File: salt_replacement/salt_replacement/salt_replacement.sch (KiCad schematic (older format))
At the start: 18 parts, among them J1 SALT chip package pins, U1 IC REG BUCK SEPIC 5V 4.5A 8SO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, U2 MAX3232

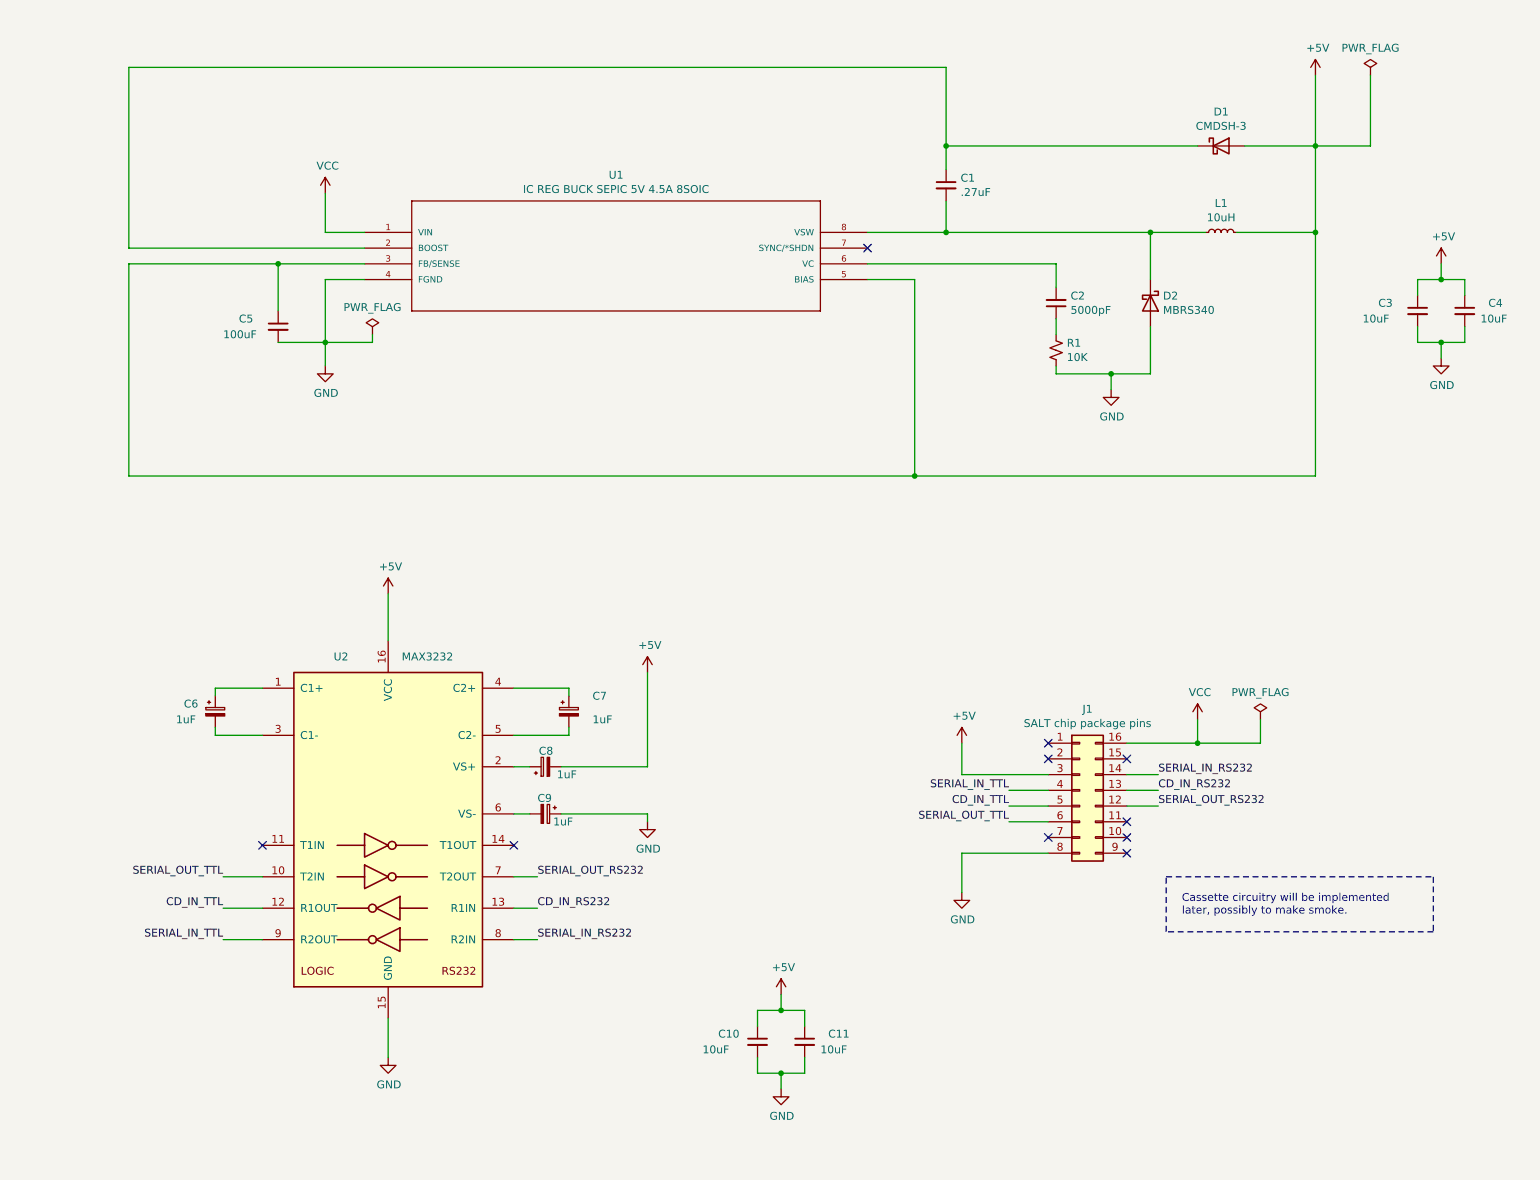
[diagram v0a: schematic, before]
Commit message: -added more components -started making the PCB
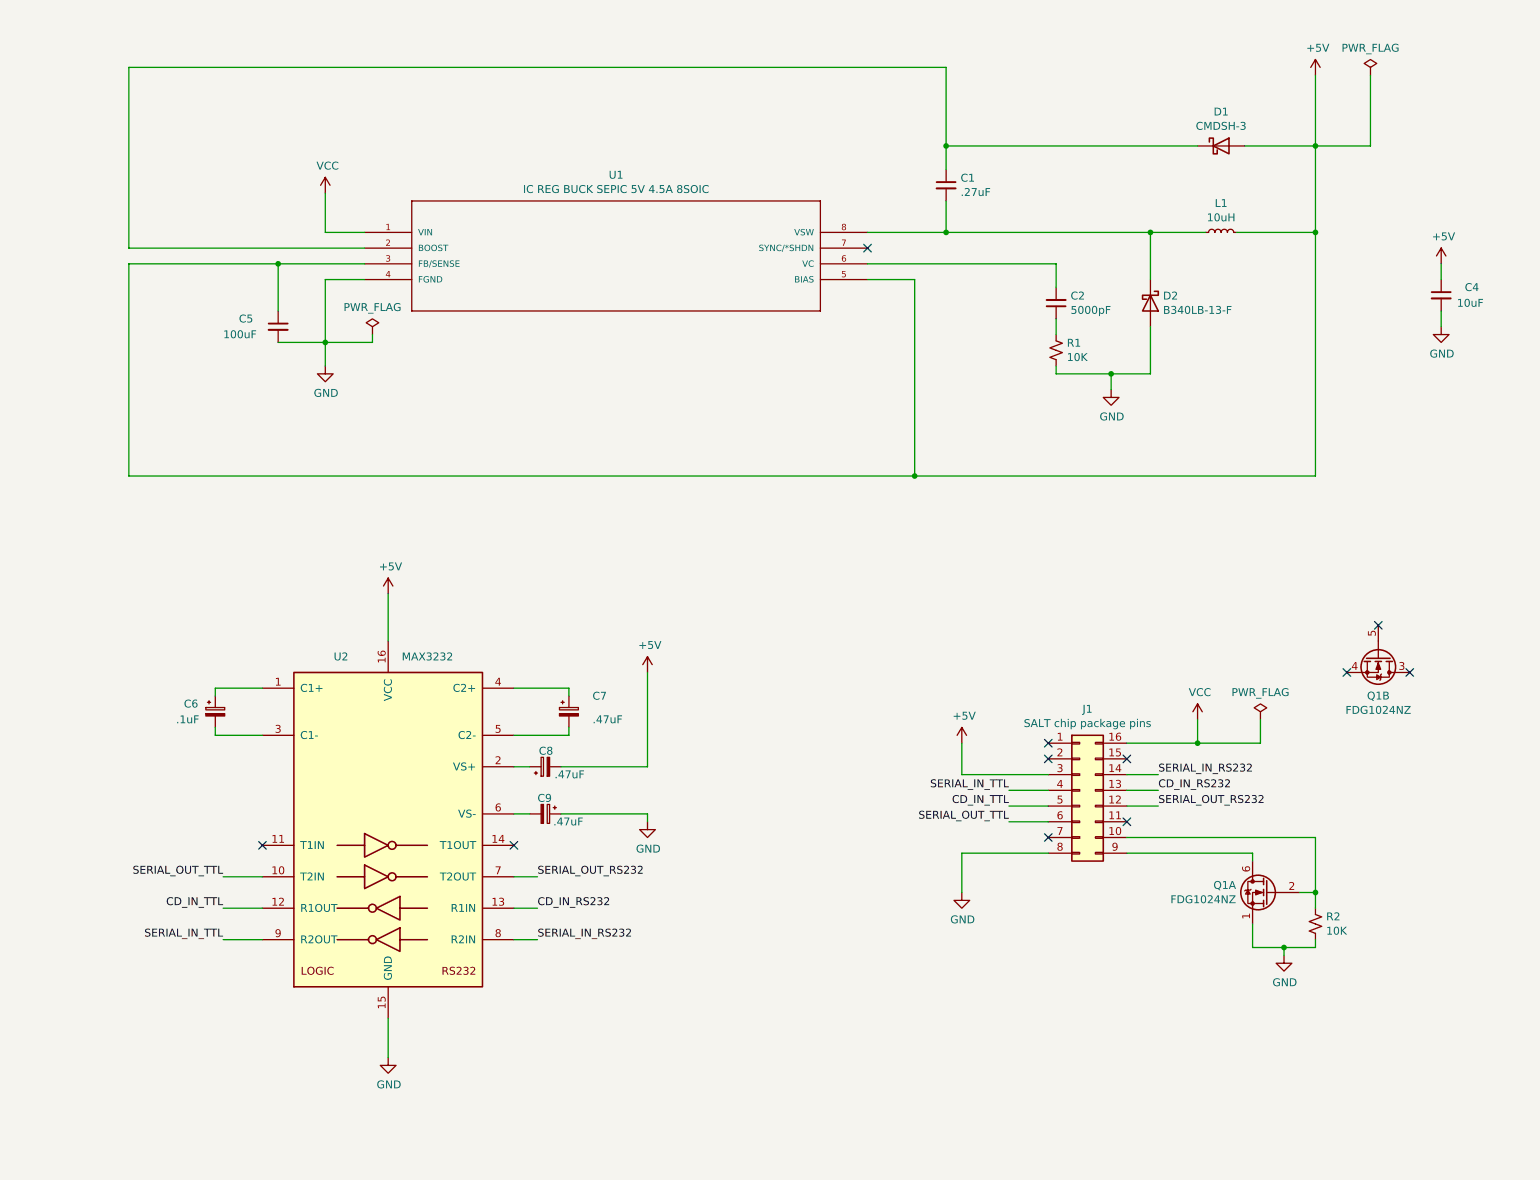
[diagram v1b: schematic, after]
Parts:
- removed C10, C11, C3: 10uF, symbol Device:C_Small
- added Q1: FDG1024NZ, Package_TO_SOT_SMD:SOT-363_SC-70-6, symbol Transistor_FET:FDG1024NZ
- added R2: 10K, Resistor_SMD:R_0805_2012Metric_Pad1.20x1.40mm_HandSolder, symbol Device:R_Small_US
- C1: footprint (none) -> Capacitor_SMD:C_1206_3216Metric_Pad1.33x1.80mm_HandSolder; Manufacturer part# (none) -> 12065C274KAT2A; Vendor (none) -> Digikey; Vendor part# (none) -> 478-1561-1-ND
- C2: footprint (none) -> Capacitor_SMD:C_0805_2012Metric_Pad1.18x1.45mm_HandSolder; Manufacturer part# (none) -> 08055C502KAT2A; Vendor (none) -> Digikey; Vendor part# (none) -> 478-10560-1-ND
- C4: footprint (none) -> Capacitor_Tantalum_SMD:CP_EIA-3216-18_Kemet-A_Pad1.58x1.35mm_HandSolder; Manufacturer part# (none) -> T491A106K010AT; Vendor (none) -> digikey; Vendor part# (none) -> 399-3684-1-ND
- C5: footprint (none) -> Capacitor_Tantalum_SMD:CP_EIA-7343-31_Kemet-D_Pad2.25x2.55mm_HandSolder; Vendor (none) -> digikey; Vendor part# (none) -> 478-9137-1-ND; manufacturer part# (none) -> TPSD107K010S0080
- C6: value 1uF -> .1uF; footprint (none) -> Capacitor_SMD:C_0603_1608Metric_Pad1.08x0.95mm_HandSolder; Manufacturer part# (none) -> CC0603KRX7R9BB104; Vendor (none) -> digikey; Vendor part# (none) -> 311-1344-1-ND
- C7, C8, C9: value 1uF -> .47uF; footprint (none) -> Capacitor_SMD:C_0603_1608Metric_Pad1.08x0.95mm_HandSolder; Manufacturer part# (none) -> C0603C474K4RACTU; Vendor (none) -> digikey; Vendor part# (none) -> 399-4922-1-ND
- D1: footprint (none) -> Diode_SMD:D_SOD-323_HandSoldering; Manufacturer part# (none) -> CMDSH-3 TR PBFREE; Vendor (none) -> Digikey; Vendor part# (none) -> 1514-CMDSH-3TRPBFREECT-ND
- D2: value MBRS340 -> B340LB-13-F; footprint (none) -> Diode_SMD:D_SMC; Manufacturer part# (none) -> B340LB-13-F; Vendor (none) -> digikey; Vendor part# (none) -> B340LB-FDICT-ND
- J1: footprint (none) -> Package_DIP:DIP-16_W7.62mm_Socket
- L1: footprint (none) -> salt_replacement:L_Sumida_CDMC6D28_7.25x6.5mm; Manufacturer part# (none) -> SRP6540-100M; Vendor (none) -> Digikey; Vendor part# (none) -> SRP6540-100MCT-ND
- R1: footprint (none) -> Resistor_SMD:R_0805_2012Metric_Pad1.20x1.40mm_HandSolder; Manufacturer part# (none) -> RK73B2ATTD103J; Vendor (none) -> digikey; Vendor part# (none) -> 2019-RK73B2ATTD103JCT-ND
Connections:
- net GND: now also Q1.1 (S), R2.2
- net at J1.10 (Pin_10): now also Q1.2 (G), R2.1
- net at J1.9 (Pin_9): now also Q1.6 (D)
- no-connect marks 10 -> 11
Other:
- note removed: "Cassette circuitry will be implemented\nlater, possibly to make smoke."
- moved on the sheet: C4

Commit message: -complete redesign -replaced all components with jclpcb stock -added non-inverting zero crossing circuit.
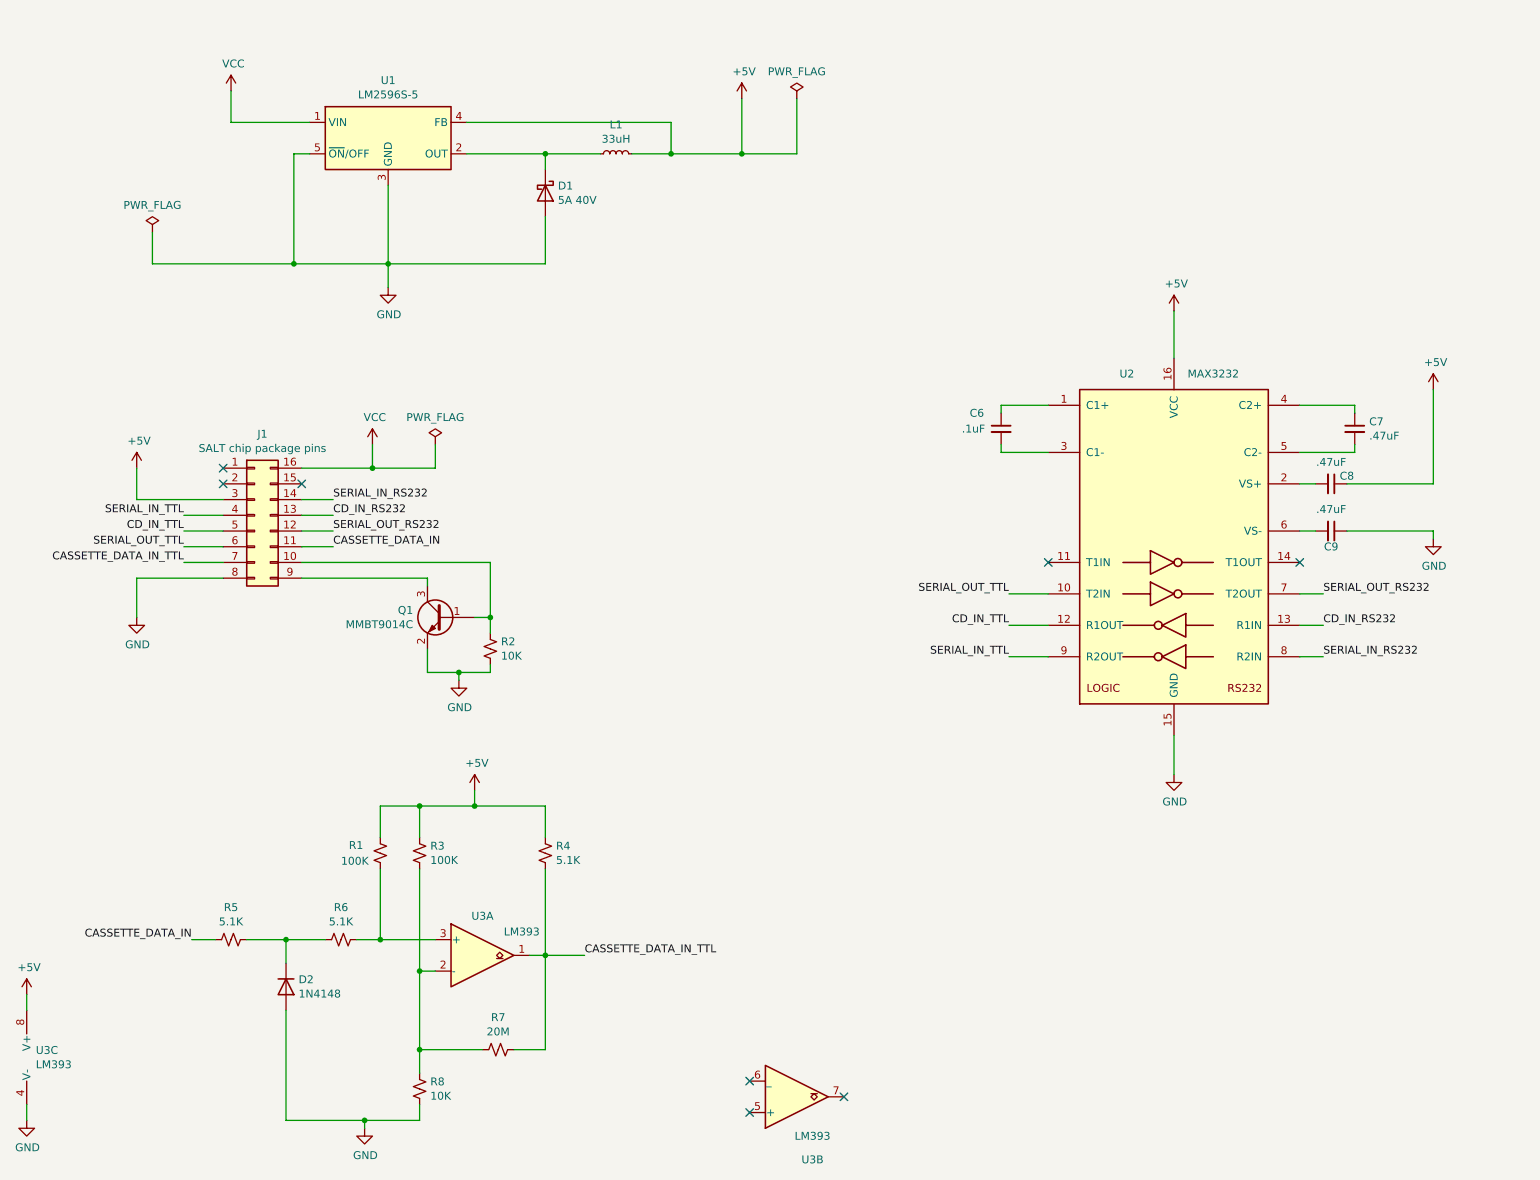
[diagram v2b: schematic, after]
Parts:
- removed C1: .27uF, Capacitor_SMD:C_1206_3216Metric_Pad1.33x1.80mm_HandSolder, symbol Device:C_Small
- removed C2: 5000pF, Capacitor_SMD:C_0805_2012Metric_Pad1.18x1.45mm_HandSolder, symbol Device:C_Small
- removed C4: 10uF, Capacitor_Tantalum_SMD:CP_EIA-3216-18_Kemet-A_Pad1.58x1.35mm_HandSolder, symbol Device:C_Small
- removed C5: 100uF, Capacitor_Tantalum_SMD:CP_EIA-7343-31_Kemet-D_Pad2.25x2.55mm_HandSolder, symbol Device:C_Small
- removed C6: .1uF, Capacitor_SMD:C_0603_1608Metric_Pad1.08x0.95mm_HandSolder, symbol Device:CP_Small
- removed C7, C8, C9: .47uF, Capacitor_SMD:C_0603_1608Metric_Pad1.08x0.95mm_HandSolder, symbol Device:CP_Small
- removed D2: B340LB-13-F, Diode_SMD:D_SMC, symbol Device:D_Schottky
- removed Q1: FDG1024NZ, Package_TO_SOT_SMD:SOT-363_SC-70-6, symbol Transistor_FET:FDG1024NZ
- removed U1: IC REG BUCK SEPIC 5V 4.5A 8SOIC, Package_SO:SO-8_3.9x4.9mm_P1.27mm, symbol coco_rip:LT1374CS8-5PBF
- added C6: .1uF, Capacitor_SMD:C_0402_1005Metric, symbol Device:C_Small
- added C7, C8, C9: .47uF, Capacitor_SMD:C_0603_1608Metric, symbol Device:C_Small
- added D2: 1N4148, Diode_SMD:D_SOD-523, symbol Diode:1N4148
- added Q1: MMBT9014C, Package_TO_SOT_SMD:SOT-23, symbol Transistor_BJT:BC818
- added R3: 100K, Resistor_SMD:R_0402_1005Metric, symbol Device:R_Small_US
- added R4, R5, R6: 5.1K, Resistor_SMD:R_0402_1005Metric, symbol Device:R_Small_US
- added R7: 20M, Resistor_SMD:R_0402_1005Metric, symbol Device:R_Small_US
- added R8: 10K, Resistor_SMD:R_0402_1005Metric, symbol Device:R_Small_US
- added U1: LM2596S-5, Package_TO_SOT_SMD:TO-263-5_TabPin3, symbol Regulator_Switching:LM2596S-5
- added U3: LM393, Package_SO:TSSOP-8_4.4x3mm_P0.65mm, symbol Comparator:LM393
- D1: value CMDSH-3 -> 5A 40V; footprint Diode_SMD:D_SOD-323_HandSoldering -> Diode_SMD:D_SMB; Manufacturer part# CMDSH-3 TR PBFREE -> SS54B; Vendor Digikey -> LCSC; Vendor part# 1514-CMDSH-3TRPBFREECT-ND -> C32513
- J1: Manufacturer part# (none) -> DNI; Vendor (none) -> DNI; Vendor part# (none) -> DNI
- L1: value 10uH -> 33uH; footprint salt_replacement:L_Sumida_CDMC6D28_7.25x6.5mm -> Inductor_SMD:L_Sumida_CDMC6D28_7.25x6.5mm; Manufacturer part# SRP6540-100M -> MHCI06030-330M-R8; Vendor Digikey -> LSCSC; Vendor part# SRP6540-100MCT-ND -> C329385
- R1: value 10K -> 100K; footprint Resistor_SMD:R_0805_2012Metric_Pad1.20x1.40mm_HandSolder -> Resistor_SMD:R_0402_1005Metric; Manufacturer part# RK73B2ATTD103J -> 0402WGF1003TCE; Vendor digikey -> LCSC; Vendor part# 2019-RK73B2ATTD103JCT-ND -> C25741
- R2: footprint Resistor_SMD:R_0805_2012Metric_Pad1.20x1.40mm_HandSolder -> Resistor_SMD:R_0402_1005Metric; Manufacturer part# RK73B2ATTD103J -> 0402WGF1002TCE; Vendor digikey -> LCSC; Vendor part# 2019-RK73B2ATTD103JCT-ND -> C25744
- U2: footprint Package_SO:SOIC-16_3.9x9.9mm_P1.27mm -> Package_SO:TSSOP-16-1EP_4.4x5mm_P0.65mm; Manufacturer paer# MAX3232IDR -> (none); Manufacturer part# (none) -> MAX3232EUE+T; Vendor digikey -> LCSC; Vendor part# 296-13098-1-ND -> C19767
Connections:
- net +5V: now also R1.1, C8.1, R3.1, R4.1, U1.4 (FB), U3.8 (V+); no longer D1.2 (A)
- net GND: now also D1.2 (A), C9.1, D2.2 (A), Q1.2 (E), R8.2, U1.3 (GND), U1.5 (~ON~/OFF), U3.4 (V-); no longer R1.2
- net VCC: now also U1.1 (VIN)
- net at U2.1 (C1+): now also C6.1
- net at U2.2 (VS+): now also C8.2
- net at U2.3 (C1-): now also C6.2
- net at U2.4 (C2+): now also C7.1
- net at U2.5 (C2-): now also C7.2
- net at U2.6 (VS-): now also C9.2
- net at J1.10 (Pin_10), R2.1: now also Q1.1 (B)
- net at J1.9 (Pin_9): now also Q1.3 (C)
- net at D1.1 (K): now also L1.1, U1.2 (OUT)
- net CASSETTE_DATA_IN: now reaches J1.11 (Pin_11)
- net CASSETTE_DATA_IN: now also R5.2
- net CASSETTE_DATA_IN_TTL: now reaches J1.7 (Pin_7)
- net CASSETTE_DATA_IN_TTL: now also R4.2, R7.1, U3.1
- new net: R3.2, R7.2, R8.1, U3.2 (-)
- new net: R1.2, R6.1, U3.3 (+)
- new net: D2.1 (K), R5.1, R6.2
- no-connect marks 11 -> 8
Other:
- moved on the sheet: J1, R2, U2

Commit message: updated BOM with available parts from jlcpcb
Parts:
- L1: Manufacturer part# MHCI06030-330M-R8 -> YSPI0740-330M; Vendor part# C329385 -> C718398
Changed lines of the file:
@@
 F 3 "https://datasheet.lcsc.com/lcsc/1912111437_Chilisin-Elec-MHCI06030-330M-R8_C329385.pdf" H 4450 1550 50  0001 C CNN
 F 4 "LSCSC" V 4450 1550 50  0001 C CNN "Vendor"
-F 5 "C329385" V 4450 1550 50  0001 C CNN "Vendor part#"
-F 6 "MHCI06030-330M-R8" V 4450 1550 50  0001 C CNN "Manufacturer part#"
+F 5 "C718398" V 4450 1550 50  0001 C CNN "Vendor part#"
+F 6 "YSPI0740-330M" V 4450 1550 50  0001 C CNN "Manufacturer part#"
 	1    4450 1550
 	0    -1   -1   0
